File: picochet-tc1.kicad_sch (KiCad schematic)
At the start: 62 parts, among them J1 Conn_01x02, J2 Conn_01x02, J3 Conn_01x04, J4 Conn_01x02, J5 Conn_02x02, J6 Conn_01x05, J7 Conn_01x03, Q1 DMT12H060LFDF, Q2 DMT12H060LFDF, SW1 SW_Push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

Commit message: Cleanup
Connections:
- no-connect marks 29 -> 63

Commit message: Small tweaks for v0.1 prototype
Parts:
- J2, J3, J4, J6: now left out of the parts list
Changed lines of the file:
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@@
 		(unit 1)
 		(exclude_from_sim no)
-		(in_bom yes)
+		(in_bom no)
 		(on_board yes)
 		(dnp no)
@@
 		(unit 1)
 		(exclude_from_sim no)
-		(in_bom yes)
+		(in_bom no)
 		(on_board yes)
 		(dnp no)
@@
 		(unit 1)
 		(exclude_from_sim no)
-		(in_bom yes)
+		(in_bom no)
 		(on_board yes)
 		(dnp no)
@@
 		(unit 1)
 		(exclude_from_sim no)
-		(in_bom yes)
-		(on_board yes)
-		(dnp no)
+		(in_bom no)
+		(on_board yes)
+		(dnp no)

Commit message: swap 10uF caps to 0805; tweak routing
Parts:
- C1, C19, C5: footprint Capacitor_SMD:C_0402_1005Metric_Pad0.74x0.62mm_HandSolder -> Capacitor_SMD:C_0805_2012Metric_Pad1.18x1.45mm_HandSolder
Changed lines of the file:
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@@
 			)
 		)
-		(property "Footprint" "Capacitor_SMD:C_0402_1005Metric_Pad0.74x0.62mm_HandSolder"
+		(property "Footprint" "Capacitor_SMD:C_0805_2012Metric_Pad1.18x1.45mm_HandSolder"
 			(at 98.7552 57.15 0)
 			(effects
@@
 			)
 		)
-		(property "Footprint" "Capacitor_SMD:C_0402_1005Metric_Pad0.74x0.62mm_HandSolder"
+		(property "Footprint" "Capacitor_SMD:C_0805_2012Metric_Pad1.18x1.45mm_HandSolder"
 			(at 354.0252 88.9 0)
 			(effects
@@
 			)
 		)
-		(property "Footprint" "Capacitor_SMD:C_0402_1005Metric_Pad0.74x0.62mm_HandSolder"
+		(property "Footprint" "Capacitor_SMD:C_0805_2012Metric_Pad1.18x1.45mm_HandSolder"
 			(at 69.5452 57.15 0)
 			(effects

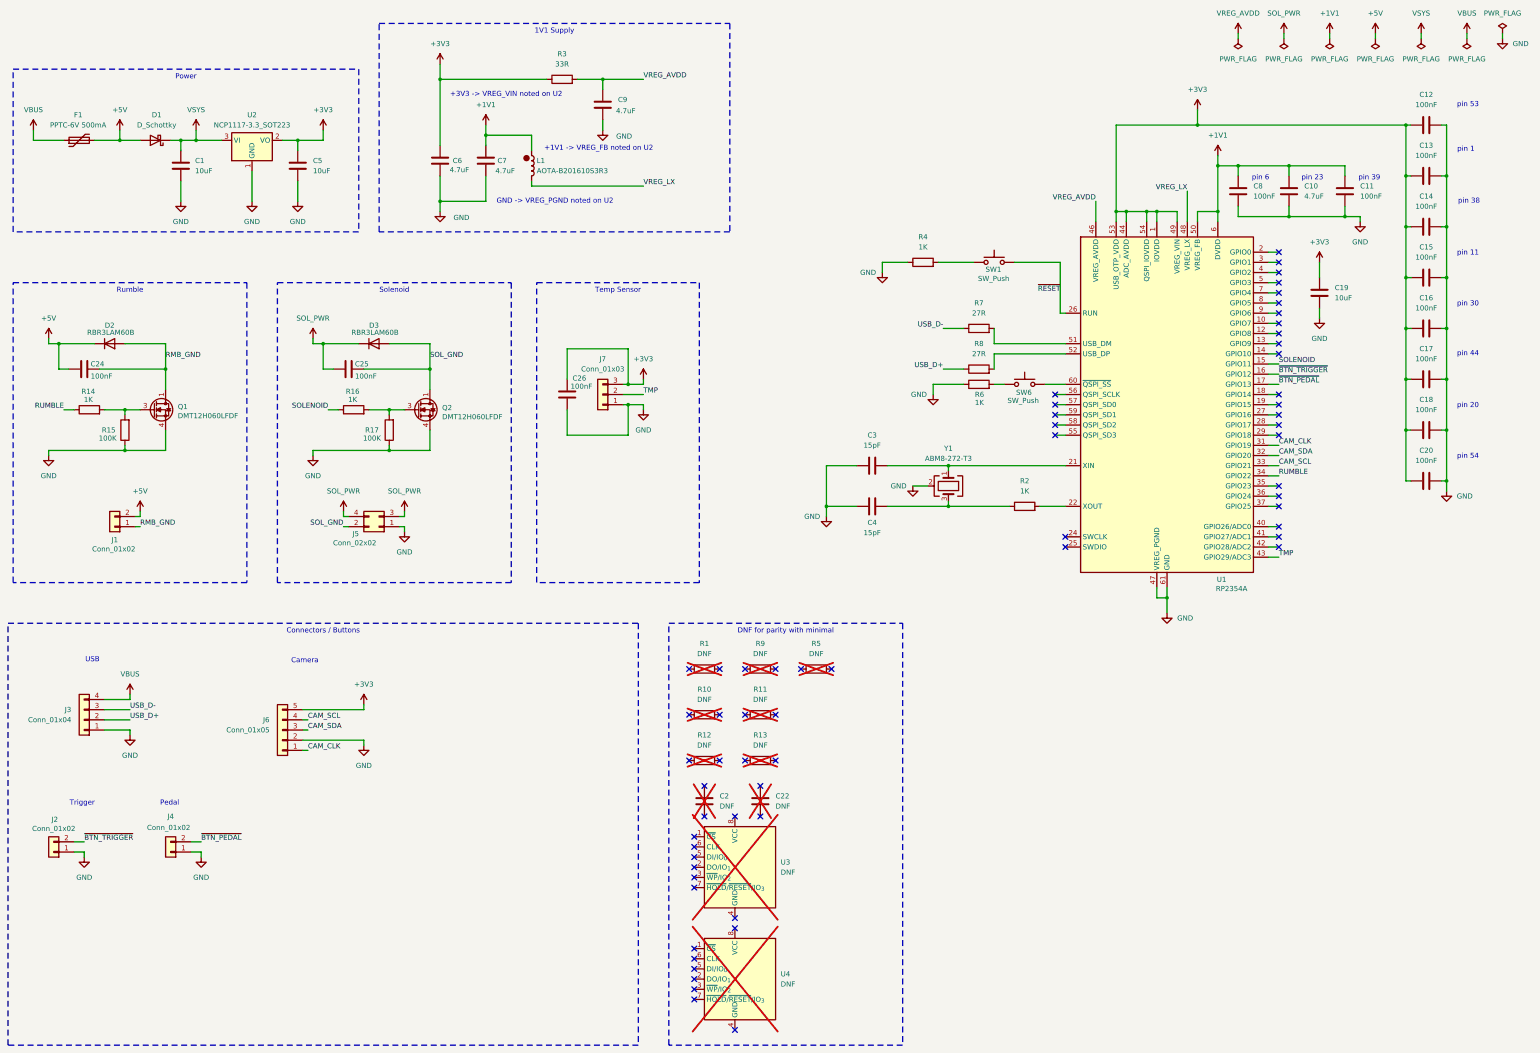
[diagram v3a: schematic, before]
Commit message: Add options for second pedal and A/B buttons
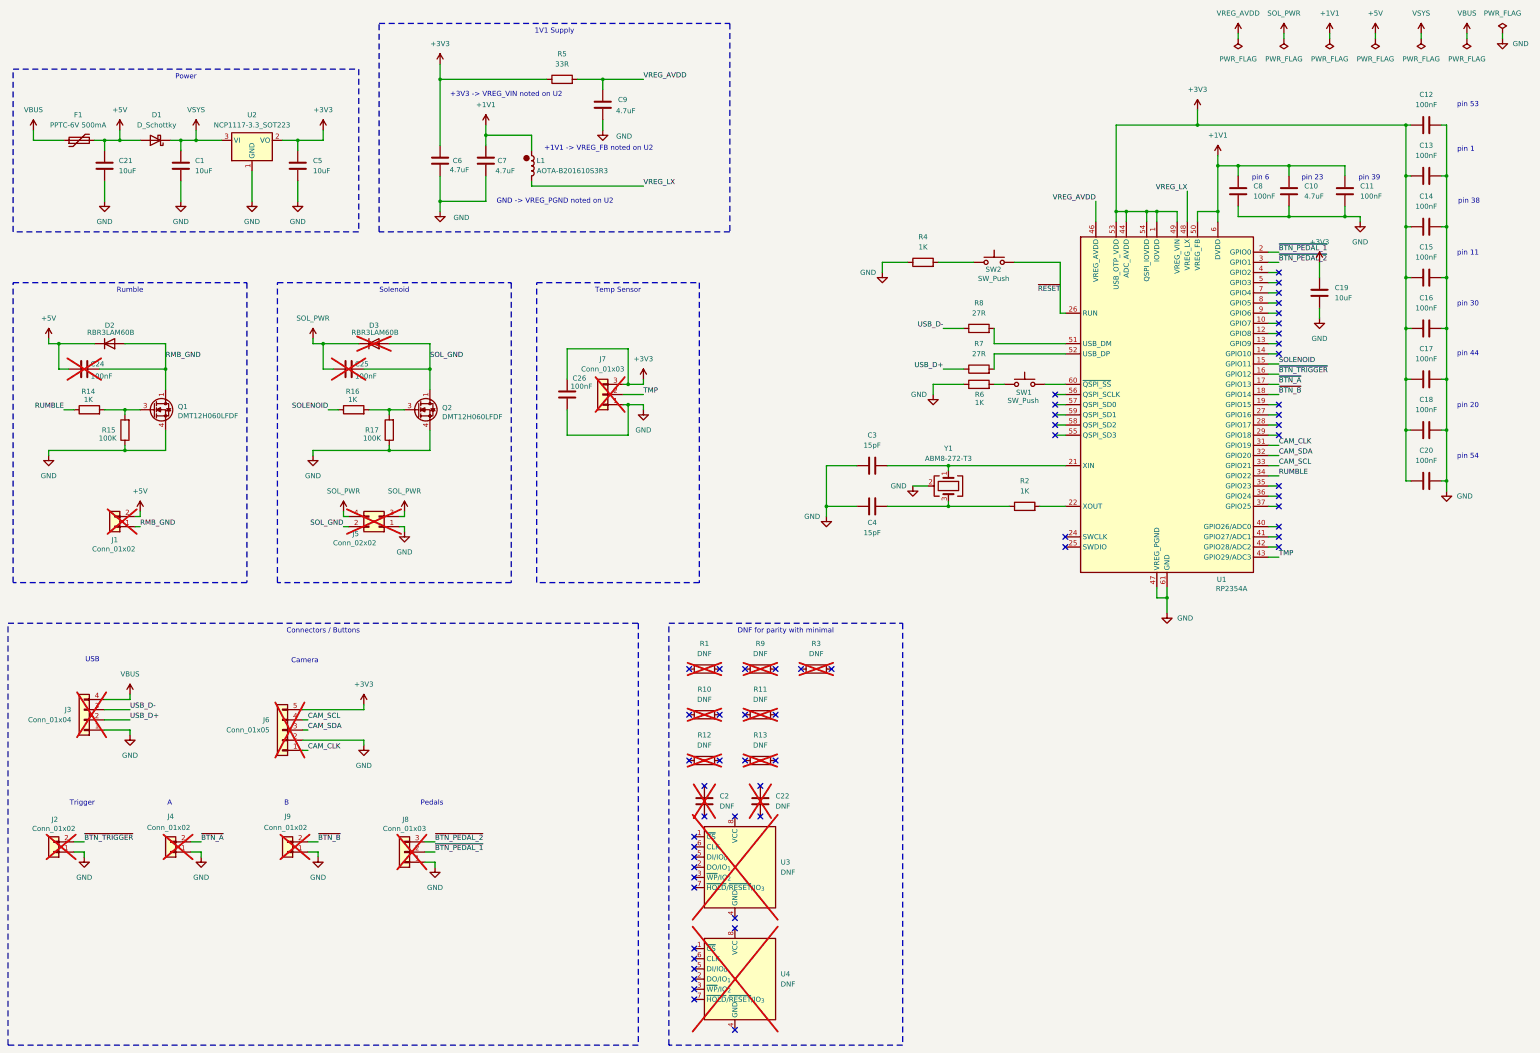
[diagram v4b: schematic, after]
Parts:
- added C21: 10uF, Capacitor_SMD:C_0805_2012Metric_Pad1.18x1.45mm_HandSolder, symbol Device:C
- added J8: Conn_01x03, Connector_PinHeader_2.54mm:PinHeader_1x03_P2.54mm_Vertical, symbol Connector_Generic:Conn_01x03
- added J9: Conn_01x02, Connector_PinHeader_2.54mm:PinHeader_1x02_P2.54mm_Vertical, symbol Connector_Generic:Conn_01x02
- C1, C19, C5: LCSC Part # (none) -> C95841
- C10, C6, C7, C9: LCSC Part # (none) -> C23733
- C11, C12, C13, C14, C15, C16, C17, C18, C20, C26, C8: LCSC Part # (none) -> C307331
- C24, C25: footprint Capacitor_SMD:C_0402_1005Metric_Pad0.74x0.62mm_HandSolder -> Capacitor_SMD:C_0805_2012Metric_Pad1.18x1.45mm_HandSolder; LCSC Part # (none) -> C307331; now not fitted
- C3, C4: LCSC Part # (none) -> C86285
- D1: LCSC Part # (none) -> C552826
- D2: LCSC Part # (none) -> C207022
- D3: LCSC Part # (none) -> C207022; now not fitted
- F1: LCSC Part # (none) -> C269104
- J1, J5, J7: now not fitted; now left out of the parts list
- J2, J4: now not fitted; now in the parts list
- J3, J6: now not fitted
- L1: LCSC Part # (none) -> C42411119
- Q1, Q2: LCSC Part # (none) -> C5711753
- R14, R16, R2, R4, R6: LCSC Part # (none) -> C11702
- R15, R17: LCSC Part # (none) -> C60491
- R5: renamed from R3; LCSC Part # (none) -> C138002
- R7, R8: LCSC Part # (none) -> C25190
- SW1: renamed from SW6; LCSC Part # (none) -> C455280
- SW2: renamed from SW1; LCSC Part # (none) -> C455280
- U1: LCSC Part # (none) -> C41378174
- U2: LCSC Part # (none) -> C26537
- Y1: LCSC Part # (none) -> ABM8-272-T3
- renumbered R5 to R3
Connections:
- net +5V: now also C21.1
- net GND: now also C21.2, J8.1 (Pin_1), J9.1 (Pin_1)
- net USB_D+: now also R7.1; no longer R8.1
- net USB_D-: now also R8.1; no longer R7.1
- net at R7.2: now also U1.52 (USB_DP); no longer U1.51 (USB_DM)
- net ~{BTN_B}: now reaches U1.18 (GPIO14)
- net ~{BTN_B}: now also J9.2 (Pin_2)
- net ~{BTN_PEDAL_1}: now reaches U1.2 (GPIO0)
- net ~{BTN_PEDAL_1}: now also J8.2 (Pin_2)
- net ~{BTN_PEDAL_2}: now reaches U1.3 (GPIO1)
- net ~{BTN_PEDAL_2}: now also J8.3 (Pin_3)
- net at R8.2: now also U1.51 (USB_DM); no longer U1.52 (USB_DP)
- net ~{BTN_PEDAL} renamed ~{BTN_A}
- no-connect marks 63 -> 60
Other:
- note added: "A"
- note added: "B"
- note added: "Pedals"
- note removed: "Pedal"
- moved on the sheet: R7, R8

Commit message: Fix LCSC part numbers for some components
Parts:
- C24, C25: LCSC Part # C307331 -> C1711
- D2, D3: LCSC Part # C207022 -> C509954
- R7, R8: LCSC Part # C25190 -> C138021
- Y1: LCSC Part # ABM8-272-T3 -> C20625731
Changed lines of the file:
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@@
 			)
 		)
-		(property "LCSC Part #" "C25190"
+		(property "LCSC Part #" "C138021"
 			(at 267.97 104.14 90)
 			(effects
@@
 			)
 		)
-		(property "LCSC Part #" "C207022"
+		(property "LCSC Part #" "C509954"
 			(at 116.84 97.79 0)
 			(effects
@@
 			)
 		)
-		(property "LCSC Part #" "C25190"
+		(property "LCSC Part #" "C138021"
 			(at 267.97 93.98 90)
 			(effects
@@
 			)
 		)
-		(property "LCSC Part #" "C307331"
+		(property "LCSC Part #" "C1711"
 			(at 110.49 104.14 90)
 			(effects
@@
 			)
 		)
-		(property "LCSC Part #" "ABM8-272-T3"
+		(property "LCSC Part #" "C20625731"
 			(at 260.35 133.35 90)
 			(effects
@@
 			)
 		)
-		(property "LCSC Part #" "C207022"
+		(property "LCSC Part #" "C509954"
 			(at 50.8 97.79 0)
 			(effects
@@
 			)
 		)
-		(property "LCSC Part #" "C307331"
+		(property "LCSC Part #" "C1711"
 			(at 44.45 104.14 90)
 			(effects
